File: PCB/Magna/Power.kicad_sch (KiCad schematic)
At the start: 40 parts, among them U601 TPS563201, U602 WS3222D, U603 AP2171W

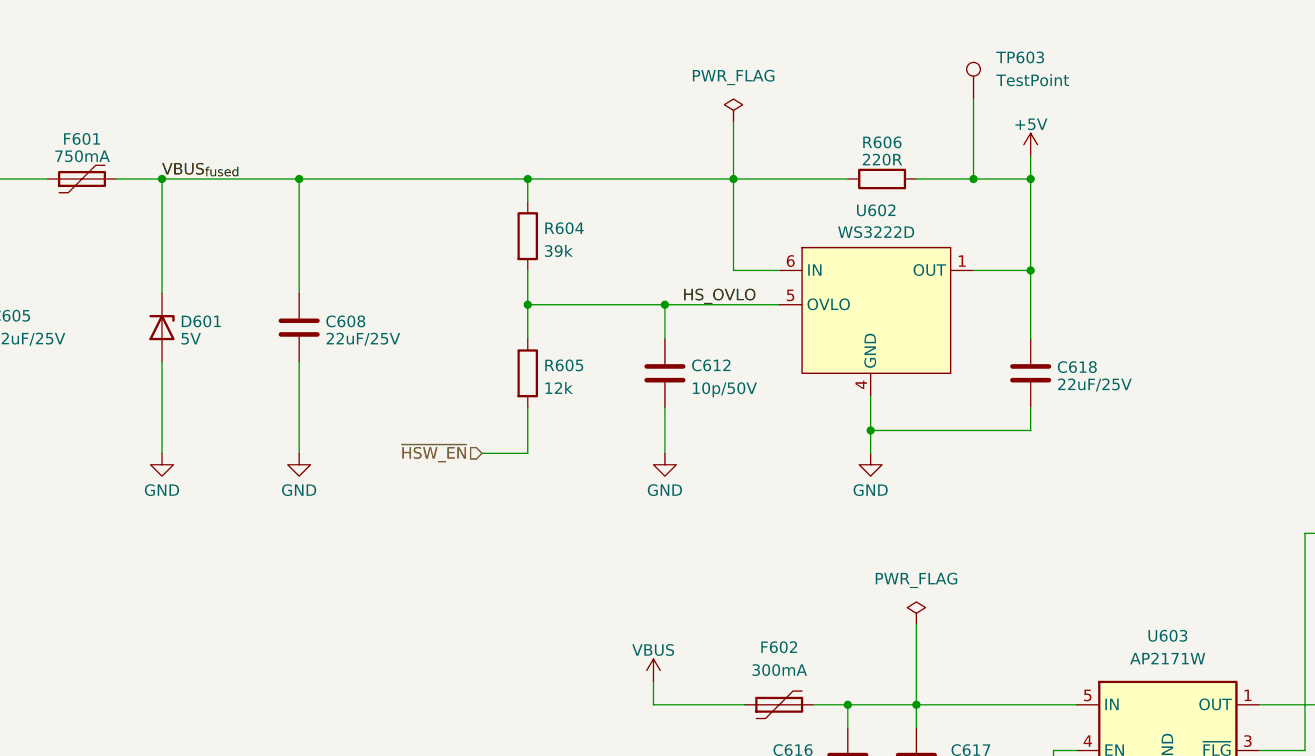
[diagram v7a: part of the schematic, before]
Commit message: Update Mainboard PCB
* Added better power ORing
* Added DRC for length matching
* Changed out components for cheaper production
* Removed some optional circuits from BOM for first prototype
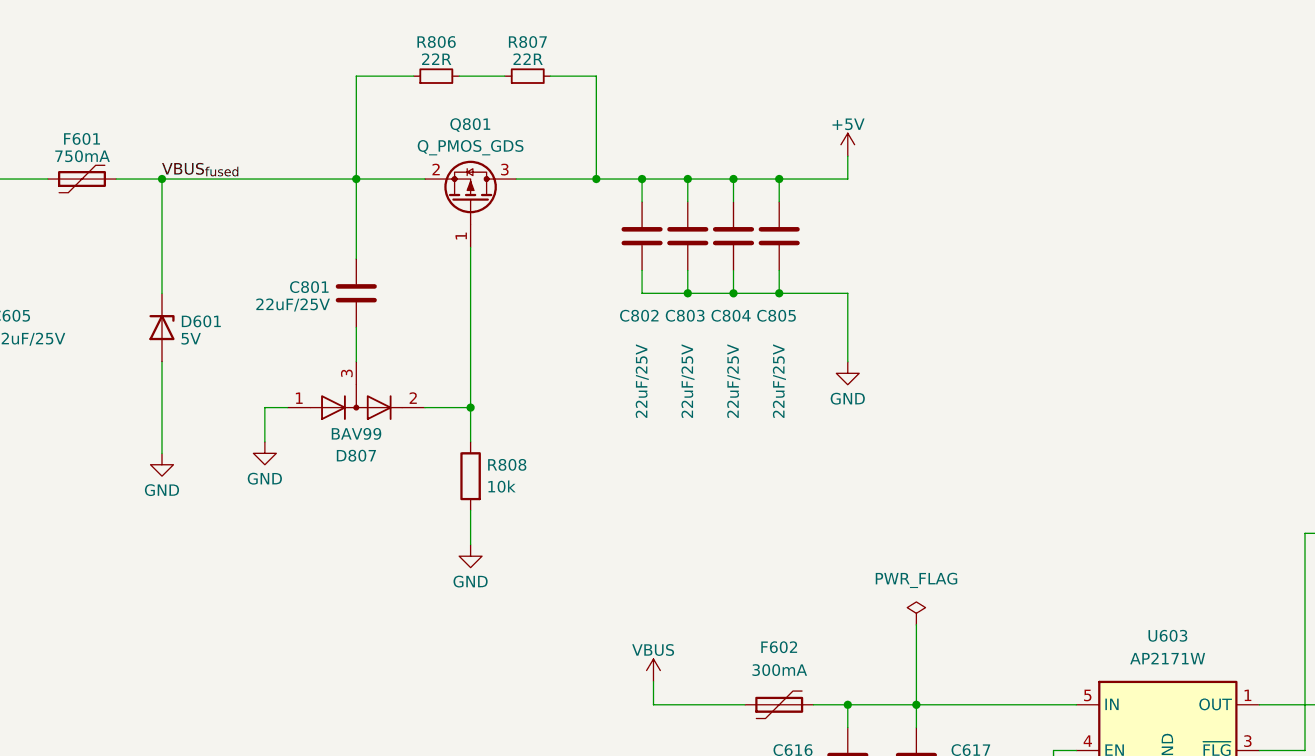
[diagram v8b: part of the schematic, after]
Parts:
- removed C608, C618: 22uF/25V, Capacitor_SMD:C_0805_2012Metric_Pad1.18x1.45mm_HandSolder, symbol Device:C
- removed C612: 10p/50V, Capacitor_SMD:C_0603_1608Metric_Pad1.08x0.95mm_HandSolder, symbol Device:C
- removed R604: 39k, Resistor_SMD:R_0805_2012Metric_Pad1.20x1.40mm_HandSolder, symbol Device:R
- removed R605: 12k, Resistor_SMD:R_0805_2012Metric_Pad1.20x1.40mm_HandSolder, symbol Device:R
- removed R606: 220R, Resistor_SMD:R_0805_2012Metric_Pad1.20x1.40mm_HandSolder, symbol Device:R
- removed TP603: TestPoint, TestPoint:TestPoint_Keystone_5000-5004_Miniature, symbol Connector:TestPoint
- removed U602: WS3222D, Package_DFN_QFN:WDFN-8-1EP_2x2mm_P0.5mm_EP0.8x1.2mm, symbol Skrooter_symbols:WS3222D
- added C801, C802, C803, C804, C805: 22uF/25V, Capacitor_SMD:C_0805_2012Metric_Pad1.18x1.45mm_HandSolder, symbol Device:C
- added D807: BAV99, Package_TO_SOT_SMD:SOT-23, symbol Diode:BAV99
- added Q801: Q_PMOS_GDS, Package_TO_SOT_SMD:SOT-23, symbol Transistor_FET:Q_PMOS_GSD
- added R806, R807: 22R, Resistor_SMD:R_0805_2012Metric_Pad1.20x1.40mm_HandSolder, symbol Device:R_Small
- added R808: 10k, Resistor_SMD:R_0805_2012Metric_Pad1.20x1.40mm_HandSolder, symbol Device:R
- D601: footprint Diode_SMD:D_MELF_Handsoldering -> Diode_SMD:D_SOD-123; LCSC C8062 -> C19077393
- TP602, TP604, TP605: now left out of the parts list
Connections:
- net +5V: now also C802.1, C803.1, C804.1, C805.1, Q801.3 (D), R807.2
- net GND: now also C802.2, C803.2, C804.2, C805.2, D807.1 (K), R808.2
- net VBUS_{fused}: now also C801.1, Q801.2 (S), R806.1
- new net: C801.2, D807.3 (K)
- new net: R806.2, R807.1
- new net: D807.2 (A), Q801.1 (G), R808.1
